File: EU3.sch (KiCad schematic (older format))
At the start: 18 parts, among them P301 HEADER_2x5_Doepfer, Q301 BC337

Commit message: Counter and Clock added to EU-3
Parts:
- removed C301, C305, C306, C310: 100uF 16v, Capacitor_THT:CP_Radial_D5.0mm_P2.50mm, symbol Device:CP
- removed C302, C303, C304, C307, C308, C309: 100n, Capacitor_SMD:C_0805_2012Metric_Pad1.15x1.40mm_HandSolder, symbol Device:C
- removed D301, D302, D303: 1N1007, Diode_SMD:D_SOD-123, symbol Device:D
- removed D304: 5v6, Diode_SMD:D_MELF-RM10_Universal_Handsoldering, symbol Device:D_Zener
- removed P301: HEADER_2x5_Doepfer, Connector_PinHeader_2.54mm:PinHeader_2x05_P2.54mm_Vertical, symbol Eurorack:HEADER_2x5_Doepfer
- removed Q301: BC337, Package_TO_SOT_THT:TO-92_Inline, symbol Transistor_BJT:BC337
- removed R301: 10k, Resistor_SMD:R_0805_2012Metric_Pad1.15x1.40mm_HandSolder, symbol Device:R
- removed R302: 0R, Resistor_SMD:R_0805_2012Metric_Pad1.15x1.40mm_HandSolder, symbol Device:R
- added C? (x5): 100n, Capacitor_SMD:C_0805_2012Metric_Pad1.15x1.40mm_HandSolder, symbol Device:C
- added C? (x3): 100uF 16v, Capacitor_THT:CP_Radial_D5.0mm_P2.50mm, symbol Device:CP
- added C?: 100uF, Capacitor_THT:CP_Radial_D5.0mm_P2.50mm, symbol Device:CP
- added C?: 10n, Capacitor_SMD:C_0805_2012Metric_Pad1.15x1.40mm_HandSolder, symbol Device:C
- added D? (x2): 1N1007, Diode_SMD:D_SOD-123, symbol Device:D
- added D? (x12): LED_Clk, LED_THT:LED_D3.0mm, symbol Device:LED
- added F?: Polyfuse, Fuse:Fuse_1206_3216Metric_Pad1.42x1.75mm_HandSolder, symbol Device:Polyfuse
- added J?: Doepfer connector, Connector_PinSocket_2.54mm:PinSocket_2x08_P2.54mm_Vertical, symbol Connector_Generic:Conn_02x08_Odd_Even
- added J?: ClockOut, AJ-Dropbox-Kicad:PJ301SM, symbol Connector:AudioJack2_Ground_Switch
- added J?: ClockIn, AJ-Dropbox-Kicad:PJ301SM, symbol Connector:AudioJack2_Ground_Switch
- added J?: Out0, AJ-Dropbox-Kicad:PJ301SM, symbol Connector:AudioJack2_Ground_Switch
- added J?: Out1, AJ-Dropbox-Kicad:PJ301SM, symbol Connector:AudioJack2_Ground_Switch
- added J?: Out2, AJ-Dropbox-Kicad:PJ301SM, symbol Connector:AudioJack2_Ground_Switch
- added J?: Out3, AJ-Dropbox-Kicad:PJ301SM, symbol Connector:AudioJack2_Ground_Switch
- added J?: Out4, AJ-Dropbox-Kicad:PJ301SM, symbol Connector:AudioJack2_Ground_Switch
- added J?: Out5, AJ-Dropbox-Kicad:PJ301SM, symbol Connector:AudioJack2_Ground_Switch
- added J?: Out6, AJ-Dropbox-Kicad:PJ301SM, symbol Connector:AudioJack2_Ground_Switch
- added J?: Out7, AJ-Dropbox-Kicad:PJ301SM, symbol Connector:AudioJack2_Ground_Switch
- added J?: Out8, AJ-Dropbox-Kicad:PJ301SM, symbol Connector:AudioJack2_Ground_Switch
- added J?: Out9, AJ-Dropbox-Kicad:PJ301SM, symbol Connector:AudioJack2_Ground_Switch
- added J?: Reset, AJ-Dropbox-Kicad:PJ301SM, symbol Connector:AudioJack2_Ground_Switch
- added R?: 3k3, Resistor_SMD:R_0805_2012Metric_Pad1.15x1.40mm_HandSolder, symbol Device:R
- added R?: 220k, Resistor_SMD:R_0805_2012Metric_Pad1.15x1.40mm_HandSolder, symbol Device:R
- added R? (x12): 680R, Resistor_SMD:R_0805_2012Metric_Pad1.15x1.40mm_HandSolder, symbol Device:R
- added R?: 10k, Resistor_SMD:R_0805_2012Metric_Pad1.15x1.40mm_HandSolder, symbol Device:R
- added RV?: 50k_freq, Potentiometer_THT:Potentiometer_China_RK09_Single_Vertical_AJ, symbol Device:R_POT
- added SW?: Run, AJ-Dropbox-Kicad:SP1MS1, symbol Switch:SW_SPDT
- added U? (x3): TL072, AJ-Dropbox-Kicad:AJ_SO-8_5.3x6.2mm_P1.27mm, symbol Amplifier_Operational:TL072
- added U?: LM555, symbol Timer:LM555
- added U?: 4017, symbol 4xxx:4017
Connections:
- net labels added: +5V, +5Vin, CV, ClockIn, ClockOut, Gate, Out0, Out1, Out2, Out3, Out4, Out5, Out6, Out7, Out8, Out9, Reset
- net labels removed: +5VL
- wire segments 57 -> 200

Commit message: change jacks
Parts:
- J301, J303, J304, J305, J306, J307, J308, J309, J310, J311, J312, J313, J314: renamed from J?; symbol Connector:AudioJack2_Ground_Switch -> Connector:AudioJack2_SwitchT
- gave numbers to parts that had none: 46

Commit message: SO8 SO16
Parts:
- U302: footprint (none) -> AJ-Dropbox-Kicad:AJ_SO-8_5.3x6.2mm_P1.27mm
- U303: footprint (none) -> Package_SO:SOIC-16_4.55x10.3mm_P1.27mm
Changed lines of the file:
@@
 F 0 "U302" H 2350 3978 50  0000 C CNN
 F 1 "LM555" H 2350 3887 50  0000 C CNN
-F 2 "" H 2350 3400 50  0001 C CNN
+F 2 "AJ-Dropbox-Kicad:AJ_SO-8_5.3x6.2mm_P1.27mm" H 2350 3400 50  0001 C CNN
 F 3 "http://www.ti.com/lit/ds/symlink/lm555.pdf" H 2350 3400 50  0001 C CNN
 	1    2350 3400
@@
 F 0 "U303" H 5650 5703 50  0000 C CNN
 F 1 "4017" H 5650 5612 50  0000 C CNN
-F 2 "" H 5650 4725 50  0001 C CNN
+F 2 "Package_SO:SOIC-16_4.55x10.3mm_P1.27mm" H 5650 4725 50  0001 C CNN
 F 3 "http://www.intersil.com/content/dam/Intersil/documents/cd40/cd4017bms-22bms.pdf" H 5650 4725 50  0001 C CNN
 	1    5650 4725

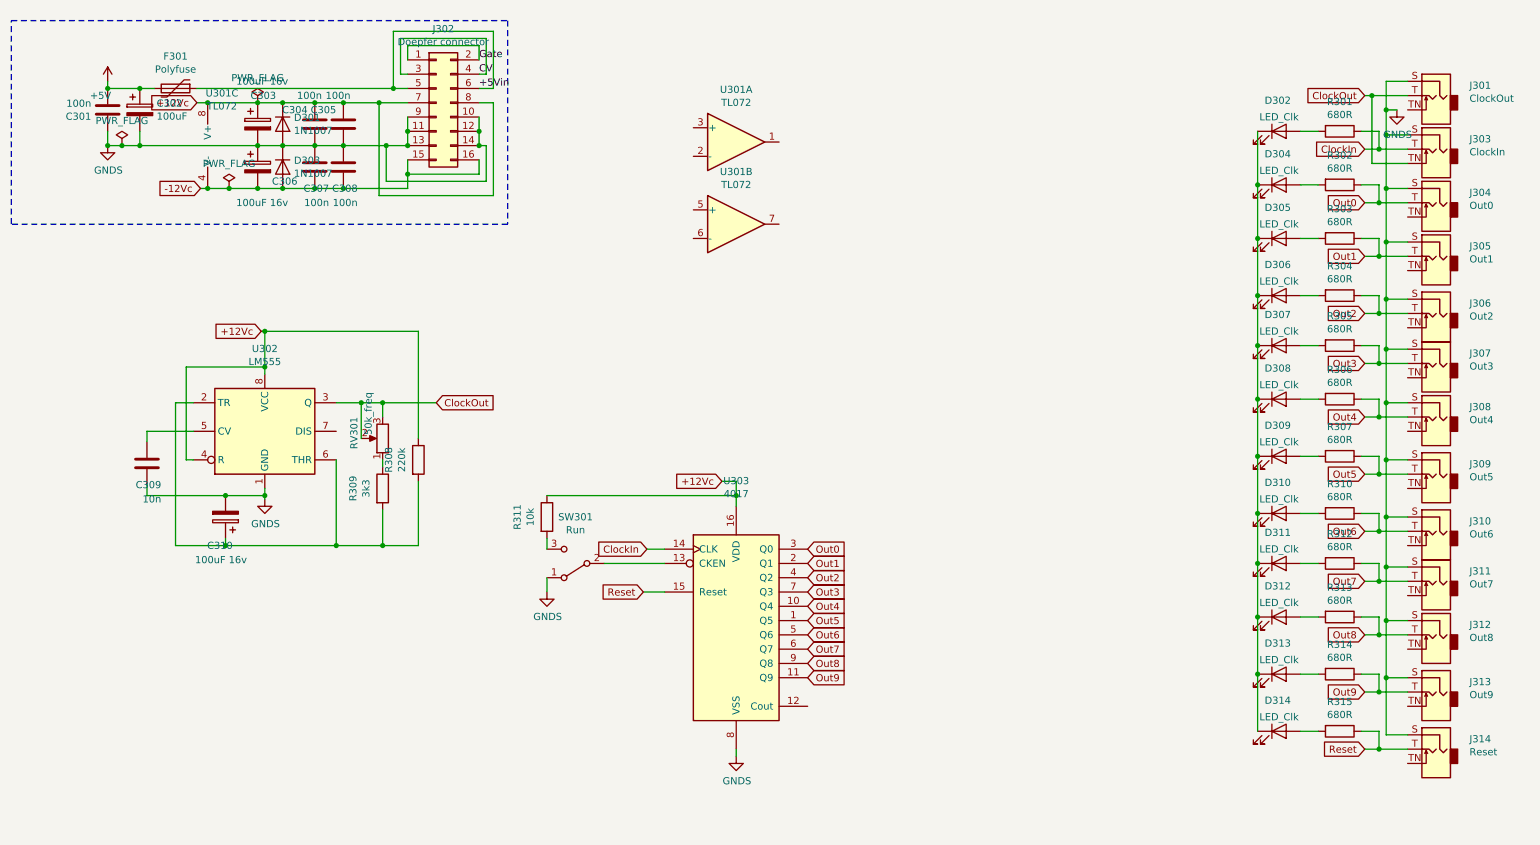
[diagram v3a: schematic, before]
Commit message: -12Vc and Opamp removed on Clock sch
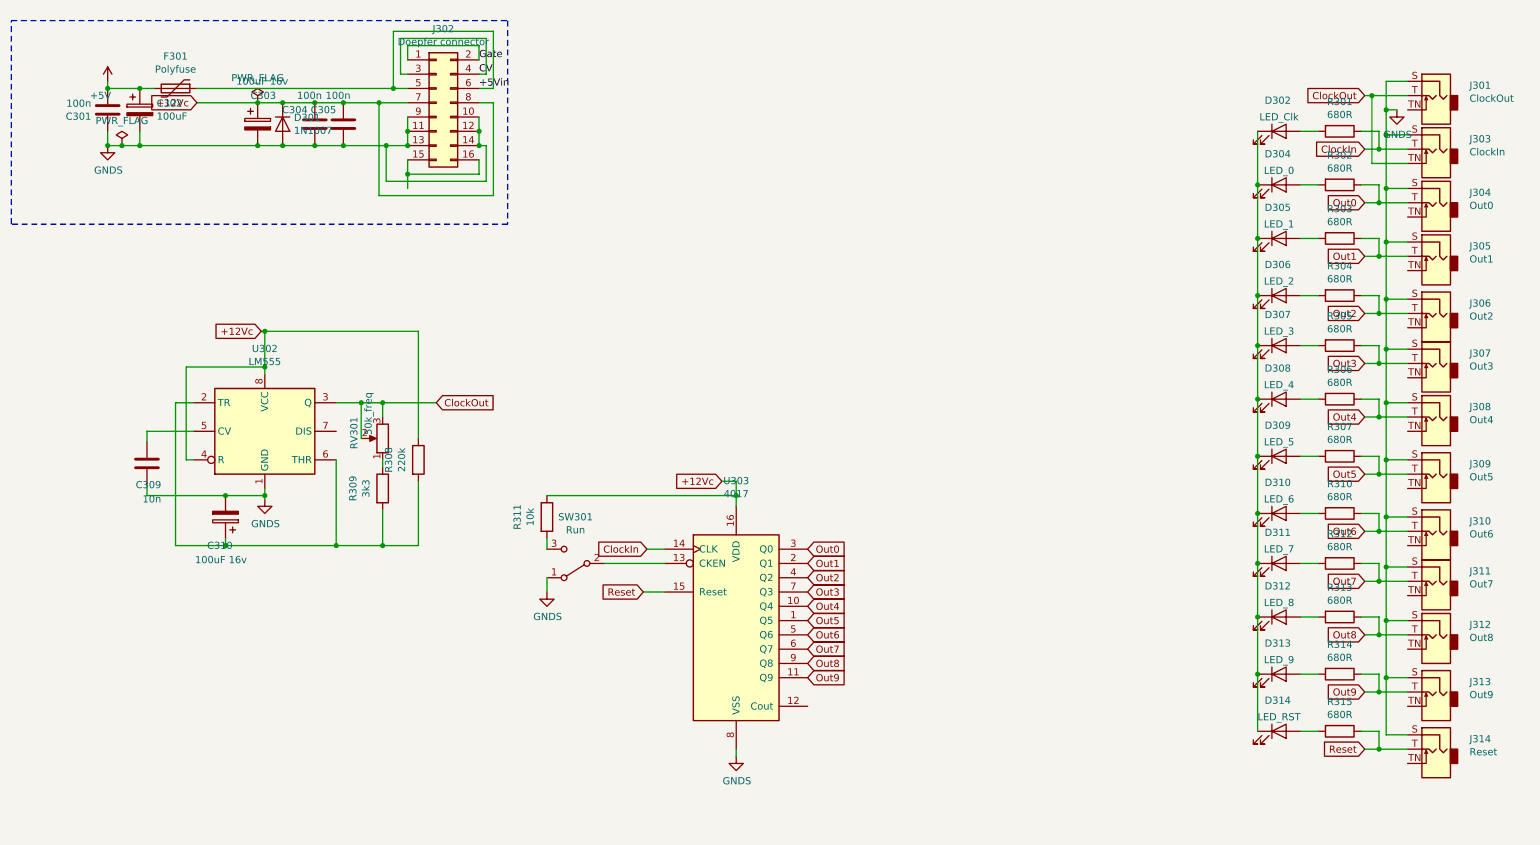
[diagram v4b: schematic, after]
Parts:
- removed C306: 100uF 16v, Capacitor_THT:CP_Radial_D5.0mm_P2.50mm, symbol Device:CP
- removed C307, C308: 100n, Capacitor_SMD:C_0805_2012Metric_Pad1.15x1.40mm_HandSolder, symbol Device:C
- removed D303: 1N1007, Diode_SMD:D_SOD-123, symbol Device:D
- removed U301: TL072, AJ-Dropbox-Kicad:AJ_SO-8_5.3x6.2mm_P1.27mm, symbol Amplifier_Operational:TL072
- D304: value LED_Clk -> LED_0
- D305: value LED_Clk -> LED_1
- D306: value LED_Clk -> LED_2
- D307: value LED_Clk -> LED_3
- D308: value LED_Clk -> LED_4
- D309: value LED_Clk -> LED_5
- D310: value LED_Clk -> LED_6
- D311: value LED_Clk -> LED_7
- D312: value LED_Clk -> LED_8
- D313: value LED_Clk -> LED_9
- D314: value LED_Clk -> LED_RST
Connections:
- net -12Vc: no longer names the net of J302.15 (Pin_15), J302.16 (Pin_16)
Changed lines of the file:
@@
 	1    0    0    -1
 $EndComp
-Text GLabel 1900 1700 0    50   Input ~ 0
--12Vc
 Text GLabel 1875 1100 0    50   Input ~ 0
 +12Vc
@@
 Connection ~ 1250 1000
 $Comp
-L Amplifier_Operational:TL072 U?
-U 3 1 5C783F9D
-P 2050 1400
-AR Path="/5C783F9D" Ref="U?"  Part="3"
-AR Path="/5C781441/5C783F9D" Ref="U301"  Part="3"
-F 0 "U301" H 2050 1767 50  0000 C CNN
-F 1 "TL072" H 2050 1676 50  0000 C CNN
-F 2 "AJ-Dropbox-Kicad:AJ_SO-8_5.3x6.2mm_P1.27mm" H 2050 1400 50  0001 C CNN
-F 3 "http://www.ti.com/lit/ds/symlink/tl071.pdf" H 2050 1400 50  0001 C CNN
-	3    2050 1400
-	1    0    0    -1
-$EndComp
-$Comp
 L Device:CP C?
 U 1 1 5C783FA4
@@
 F 3 "~" H 2300 1250 50  0001 C CNN
 	1    2300 1250
-	1    0    0    -1
-$EndComp
-$Comp
-L Device:CP C?
-U 1 1 5C783FAB
-P 2300 1550
-AR Path="/5C783FAB" Ref="C?"  Part="1"
-AR Path="/5C781441/5C783FAB" Ref="C306"  Part="1"
-F 0 "C306" H 2400 1450 50  0000 L CNN
-F 1 "100uF 16v" H 2150 1300 50  0000 L CNN
-F 2 "Capacitor_THT:CP_Radial_D5.0mm_P2.50mm" H 2338 1400 50  0001 C CNN
-F 3 "~" H 2300 1550 50  0001 C CNN
-	1    2300 1550
 	1    0    0    -1
 $EndComp
@@
 	-1   0    0    1
 $EndComp
-$Comp
-L Device:C C?
-U 1 1 5C783FC2
-P 2700 1550
-AR Path="/5C783FC2" Ref="C?"  Part="1"
-AR Path="/5C781441/5C783FC2" Ref="C307"  Part="1"
-F 0 "C307" H 2600 1700 50  0000 L CNN
-F 1 "100n" H 2600 1800 50  0000 L CNN
-F 2 "Capacitor_SMD:C_0805_2012Metric_Pad1.15x1.40mm_HandSolder" H 2738 1400 50  0001 C CNN
-F 3 "~" H 2700 1550 50  0001 C CNN
-	1    2700 1550
-	-1   0    0    1
-$EndComp
 Wire Wire Line
 	2300 1400 2475 1400
@@
 	2300 1100 2475 1100
 Connection ~ 2300 1100
-Wire Wire Line
-	2300 1700 2475 1700
-Connection ~ 2300 1700
 $Comp
 L Connector_Generic:Conn_02x08_Odd_Even J?
@@
 Wire Wire Line
 	3350 1200 3350 1300
-Connection ~ 2700 1700
 Wire Wire Line
 	3350 800  3350 700
@@
 	3350 1700 3350 1600
 Connection ~ 3350 1600
-Wire Wire Line
-	2700 1700 2900 1700
 Wire Wire Line
 	3950 1100 3950 1750
@@
 	1    0    0    -1
 $EndComp
-$Comp
-L power:PWR_FLAG #FLG?
-U 1 1 5C78400B
-P 2100 1700
-AR Path="/5C78400B" Ref="#FLG?"  Part="1"
-AR Path="/5C781441/5C78400B" Ref="#FLG0105"  Part="1"
-F 0 "#FLG0105" H 2100 1775 50  0001 C CNN
-F 1 "PWR_FLAG" H 2100 1874 50  0000 C CNN
-F 2 "" H 2100 1700 50  0001 C CNN
-F 3 "~" H 2100 1700 50  0001 C CNN
-	1    2100 1700
-	1    0    0    -1
-$EndComp
-Connection ~ 2100 1700
-Wire Wire Line
-	2100 1700 2300 1700
 Text Label 3850 800  0    50   ~ 0
 Gate
 Text Label 3850 900  0    50   ~ 0
 CV
-Wire Wire Line
-	1900 1700 1950 1700
-Connection ~ 1950 1700
-Wire Wire Line
-	1875 1100 1950 1100
-Connection ~ 1950 1100
-$Comp
-L Device:C C?
-U 1 1 5C78401C
-P 2900 1550
-AR Path="/5C78401C" Ref="C?"  Part="1"
-AR Path="/5C781441/5C78401C" Ref="C308"  Part="1"
-F 0 "C308" H 2800 1700 50  0000 L CNN
-F 1 "100n" H 2800 1800 50  0000 L CNN
-F 2 "Capacitor_SMD:C_0805_2012Metric_Pad1.15x1.40mm_HandSolder" H 2938 1400 50  0001 C CNN
-F 3 "~" H 2900 1550 50  0001 C CNN
-	1    2900 1550
-	-1   0    0    1
-$EndComp
 $Comp
 L Device:C C?
@@
 Wire Wire Line
 	2475 1400 2700 1400
-$Comp
-L Device:D D?
-U 1 1 5C784040
-P 2475 1550
-AR Path="/5C784040" Ref="D?"  Part="1"
-AR Path="/5C781441/5C784040" Ref="D303"  Part="1"
-F 0 "D303" V 2429 1629 50  0000 L CNN
-F 1 "1N1007" V 2520 1629 50  0000 L CNN
-F 2 "Diode_SMD:D_SOD-123" H 2475 1550 50  0001 C CNN
-F 3 "~" H 2475 1550 50  0001 C CNN
-	1    2475 1550
-	0    1    1    0
-$EndComp
-Connection ~ 2475 1700
-Wire Wire Line
-	2475 1700 2700 1700
-Connection ~ 2900 1700
 Connection ~ 2900 1400
 Connection ~ 2900 1100
@@
 	2900 1100 3150 1100
 Wire Wire Line
-	2900 1700 3350 1700
-Wire Wire Line
 	2900 1400 3200 1400
 Wire Wire Line
@@
 Wire Notes Line
 	4050 525  4050 1950
-Wire Wire Line
-	1950 1700 2100 1700
-Wire Wire Line
-	1950 1100 2300 1100
-$Comp
-L Amplifier_Operational:TL072 U?
-U 1 1 5C7ADEA8
-P 5650 1375
-AR Path="/5C7ADEA8" Ref="U?"  Part="3"
-AR Path="/5C781441/5C7ADEA8" Ref="U301"  Part="1"
-F 0 "U301" H 5650 1742 50  0000 C CNN
-F 1 "TL072" H 5650 1651 50  0000 C CNN
-F 2 "AJ-Dropbox-Kicad:AJ_SO-8_5.3x6.2mm_P1.27mm" H 5650 1375 50  0001 C CNN
-F 3 "http://www.ti.com/lit/ds/symlink/tl071.pdf" H 5650 1375 50  0001 C CNN
-	1    5650 1375
-	1    0    0    -1
-$EndComp
-$Comp
-L Amplifier_Operational:TL072 U?
-U 2 1 5C7ADF1C
-P 5650 1950
-AR Path="/5C7ADF1C" Ref="U?"  Part="3"
-AR Path="/5C781441/5C7ADF1C" Ref="U301"  Part="2"
-F 0 "U301" H 5650 2317 50  0000 C CNN
-F 1 "TL072" H 5650 2226 50  0000 C CNN
-F 2 "AJ-Dropbox-Kicad:AJ_SO-8_5.3x6.2mm_P1.27mm" H 5650 1950 50  0001 C CNN
-F 3 "http://www.ti.com/lit/ds/symlink/tl071.pdf" H 5650 1950 50  0001 C CNN
-	2    5650 1950
-	1    0    0    -1
-$EndComp
 $Comp
 L Timer:LM555 U302
@@
 AR Path="/5C781441/5C827C40" Ref="D304"  Part="1"
 F 0 "D304" H 9441 1891 50  0000 C CNN
-F 1 "LED_Clk" H 9450 1775 50  0000 C CNN
+F 1 "LED_0" H 9450 1775 50  0000 C CNN
 F 2 "LED_THT:LED_D3.0mm" H 9450 1675 50  0001 C CNN
 F 3 "~" H 9450 1675 50  0001 C CNN
@@
 AR Path="/5C781441/5C831A2E" Ref="D305"  Part="1"
 F 0 "D305" H 9441 2266 50  0000 C CNN
-F 1 "LED_Clk" H 9450 2150 50  0000 C CNN
+F 1 "LED_1" H 9450 2150 50  0000 C CNN
 F 2 "LED_THT:LED_D3.0mm" H 9450 2050 50  0001 C CNN
 F 3 "~" H 9450 2050 50  0001 C CNN
@@
 AR Path="/5C781441/5C8355A4" Ref="D306"  Part="1"
 F 0 "D306" H 9441 2666 50  0000 C CNN
-F 1 "LED_Clk" H 9450 2550 50  0000 C CNN
+F 1 "LED_2" H 9450 2550 50  0000 C CNN
 F 2 "LED_THT:LED_D3.0mm" H 9450 2450 50  0001 C CNN
 F 3 "~" H 9450 2450 50  0001 C CNN
@@
 AR Path="/5C781441/5C83D86B" Ref="D307"  Part="1"
 F 0 "D307" H 9441 3016 50  0000 C CNN
-F 1 "LED_Clk" H 9450 2900 50  0000 C CNN
+F 1 "LED_3" H 9450 2900 50  0000 C CNN
 F 2 "LED_THT:LED_D3.0mm" H 9450 2800 50  0001 C CNN
 F 3 "~" H 9450 2800 50  0001 C CNN
@@
 AR Path="/5C781441/5C83D87E" Ref="D308"  Part="1"
 F 0 "D308" H 9441 3391 50  0000 C CNN
-F 1 "LED_Clk" H 9450 3275 50  0000 C CNN
+F 1 "LED_4" H 9450 3275 50  0000 C CNN
 F 2 "LED_THT:LED_D3.0mm" H 9450 3175 50  0001 C CNN
 F 3 "~" H 9450 3175 50  0001 C CNN
@@
 AR Path="/5C781441/5C83D891" Ref="D309"  Part="1"
 F 0 "D309" H 9441 3791 50  0000 C CNN
-F 1 "LED_Clk" H 9450 3675 50  0000 C CNN
+F 1 "LED_5" H 9450 3675 50  0000 C CNN
 F 2 "LED_THT:LED_D3.0mm" H 9450 3575 50  0001 C CNN
 F 3 "~" H 9450 3575 50  0001 C CNN
@@
 AR Path="/5C781441/5C843B43" Ref="D310"  Part="1"
 F 0 "D310" H 9441 4191 50  0000 C CNN
-F 1 "LED_Clk" H 9450 4075 50  0000 C CNN
+F 1 "LED_6" H 9450 4075 50  0000 C CNN
 F 2 "LED_THT:LED_D3.0mm" H 9450 3975 50  0001 C CNN
 F 3 "~" H 9450 3975 50  0001 C CNN
@@
 AR Path="/5C781441/5C843B6F" Ref="D311"  Part="1"
 F 0 "D311" H 9441 4541 50  0000 C CNN
-F 1 "LED_Clk" H 9450 4425 50  0000 C CNN
+F 1 "LED_7" H 9450 4425 50  0000 C CNN
 F 2 "LED_THT:LED_D3.0mm" H 9450 4325 50  0001 C CNN
 F 3 "~" H 9450 4325 50  0001 C CNN
@@
 AR Path="/5C781441/5C843B82" Ref="D312"  Part="1"
 F 0 "D312" H 9441 4916 50  0000 C CNN
-F 1 "LED_Clk" H 9450 4800 50  0000 C CNN
+F 1 "LED_8" H 9450 4800 50  0000 C CNN
 F 2 "LED_THT:LED_D3.0mm" H 9450 4700 50  0001 C CNN
 F 3 "~" H 9450 4700 50  0001 C CNN
@@
 AR Path="/5C781441/5C843B95" Ref="D313"  Part="1"
 F 0 "D313" H 9441 5316 50  0000 C CNN
-F 1 "LED_Clk" H 9450 5200 50  0000 C CNN
+F 1 "LED_9" H 9450 5200 50  0000 C CNN
 F 2 "LED_THT:LED_D3.0mm" H 9450 5100 50  0001 C CNN
 F 3 "~" H 9450 5100 50  0001 C CNN
@@
 AR Path="/5C781441/5C8555D1" Ref="D314"  Part="1"
 F 0 "D314" H 9441 5716 50  0000 C CNN
-F 1 "LED_Clk" H 9450 5600 50  0000 C CNN
+F 1 "LED_RST" H 9450 5600 50  0000 C CNN
 F 2 "LED_THT:LED_D3.0mm" H 9450 5500 50  0001 C CNN
 F 3 "~" H 9450 5500 50  0001 C CNN
@@
 Wire Wire Line
 	4325 4525 4325 4425
+Wire Wire Line
+	1875 1100 2300 1100
 $EndSCHEMATC

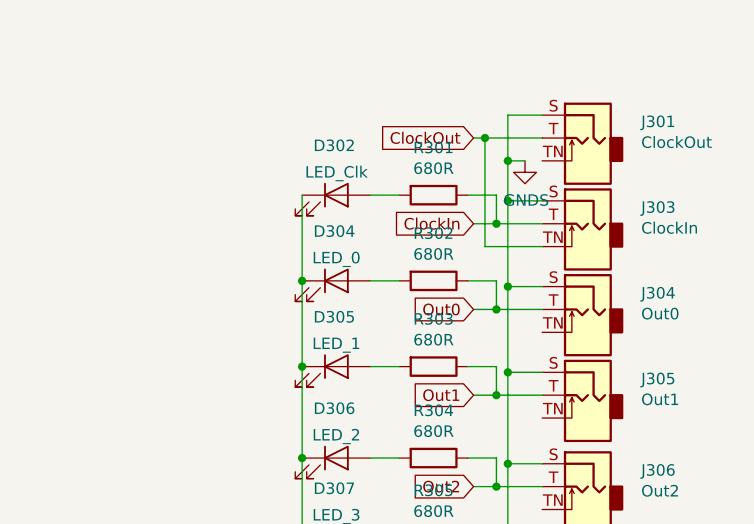
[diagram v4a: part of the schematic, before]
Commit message: Large components placed EU3
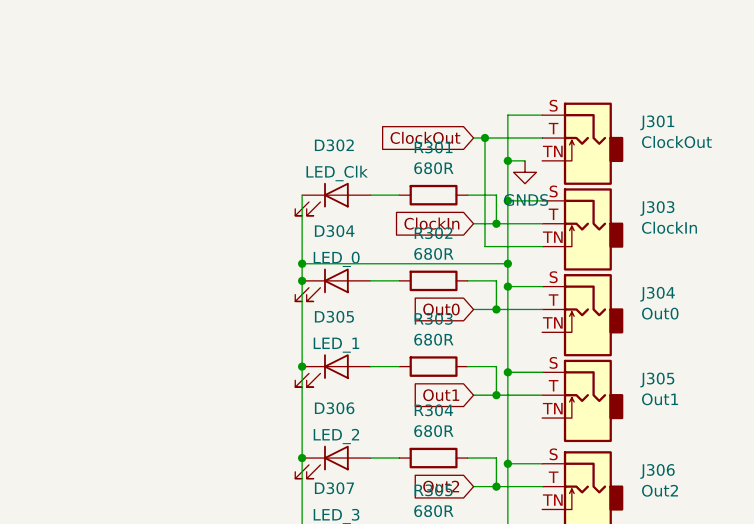
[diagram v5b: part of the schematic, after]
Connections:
- net GNDS: now also D302.1 (K), D304.1 (K), D305.1 (K), D306.1 (K), D307.1 (K), D308.1 (K), D309.1 (K), D310.1 (K), D311.1 (K), D312.1 (K), D313.1 (K), D314.1 (K)
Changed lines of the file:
@@
 $EndComp
 Wire Wire Line
-	10200 1325 10200 1700
+	10200 1325 10200 1600
 Wire Wire Line
 	10200 1700 10350 1700
@@
 Wire Wire Line
 	10150 2575 10050 2575
-Wire Wire Line
-	9300 1300 9300 1675
 Connection ~ 9300 1675
 Wire Wire Line
@@
 Wire Wire Line
 	1875 1100 2300 1100
+Wire Wire Line
+	10200 1600 9300 1600
+Wire Wire Line
+	9300 1300 9300 1600
+Connection ~ 10200 1600
+Wire Wire Line
+	10200 1600 10200 1700
+Connection ~ 9300 1600
+Wire Wire Line
+	9300 1600 9300 1675
 $EndSCHEMATC
